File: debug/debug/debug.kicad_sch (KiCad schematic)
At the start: 2 parts

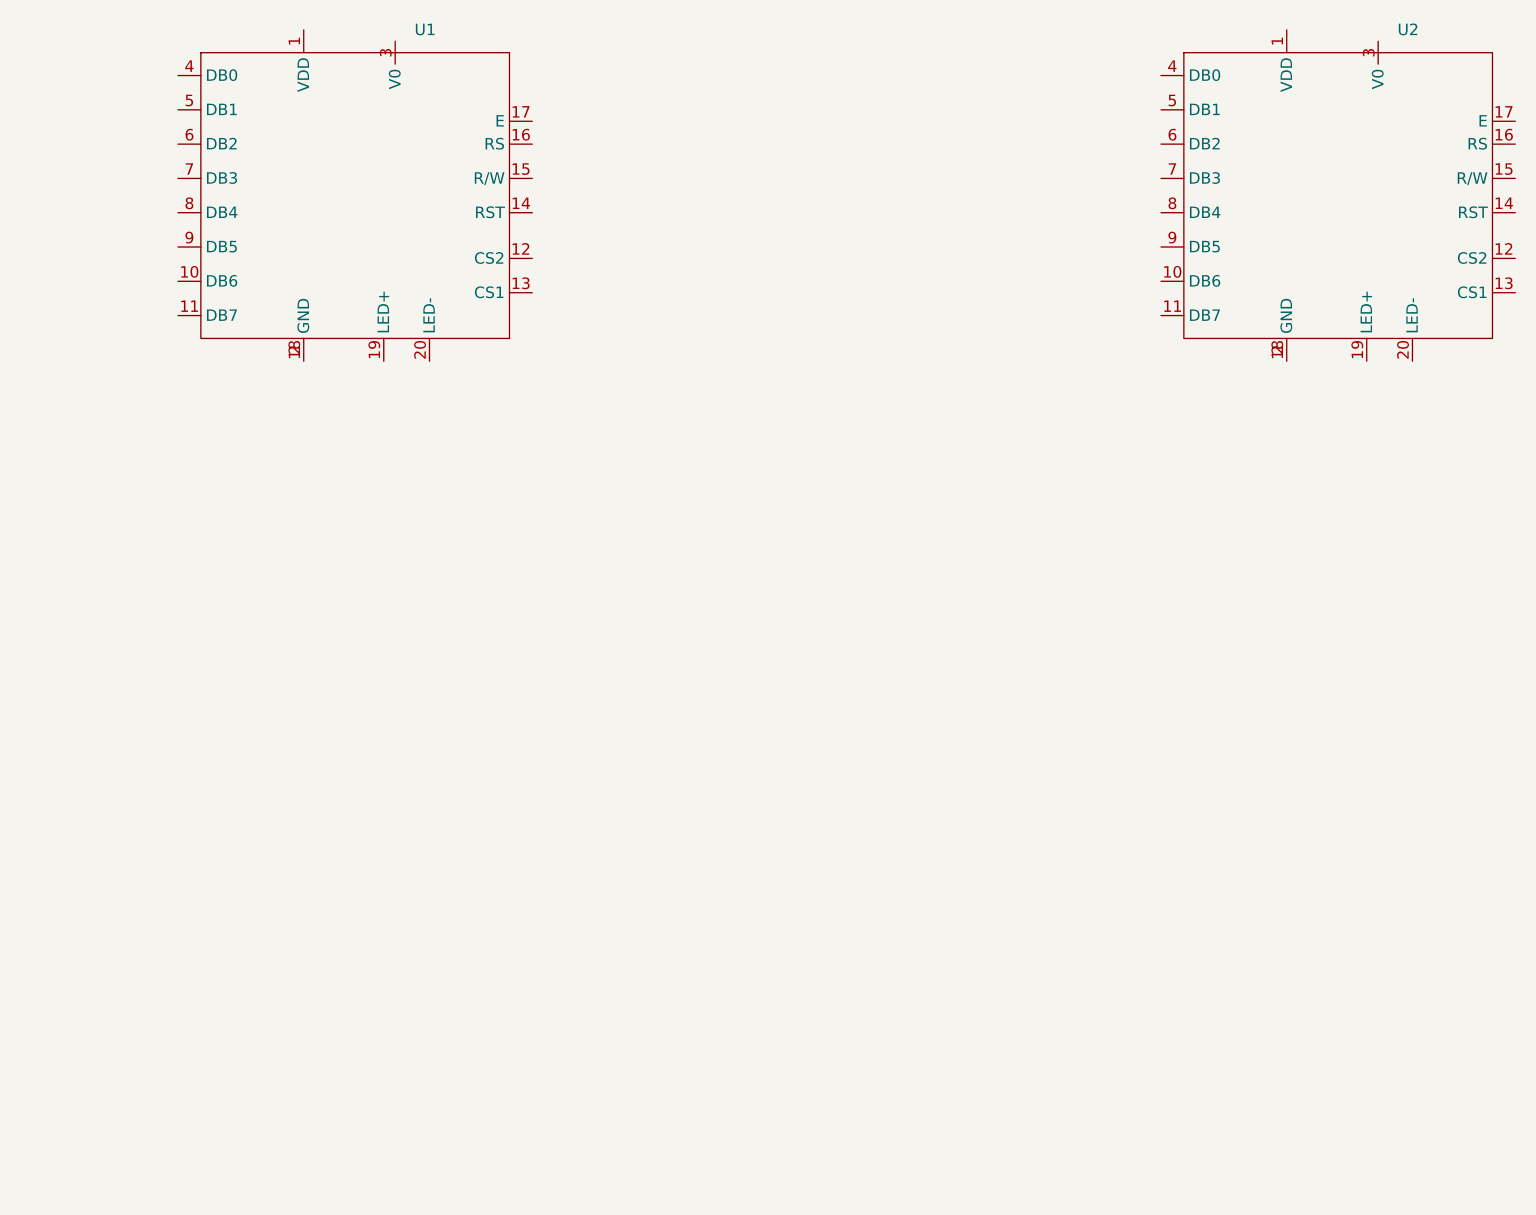
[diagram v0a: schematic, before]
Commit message: Added hierarchial blocks.
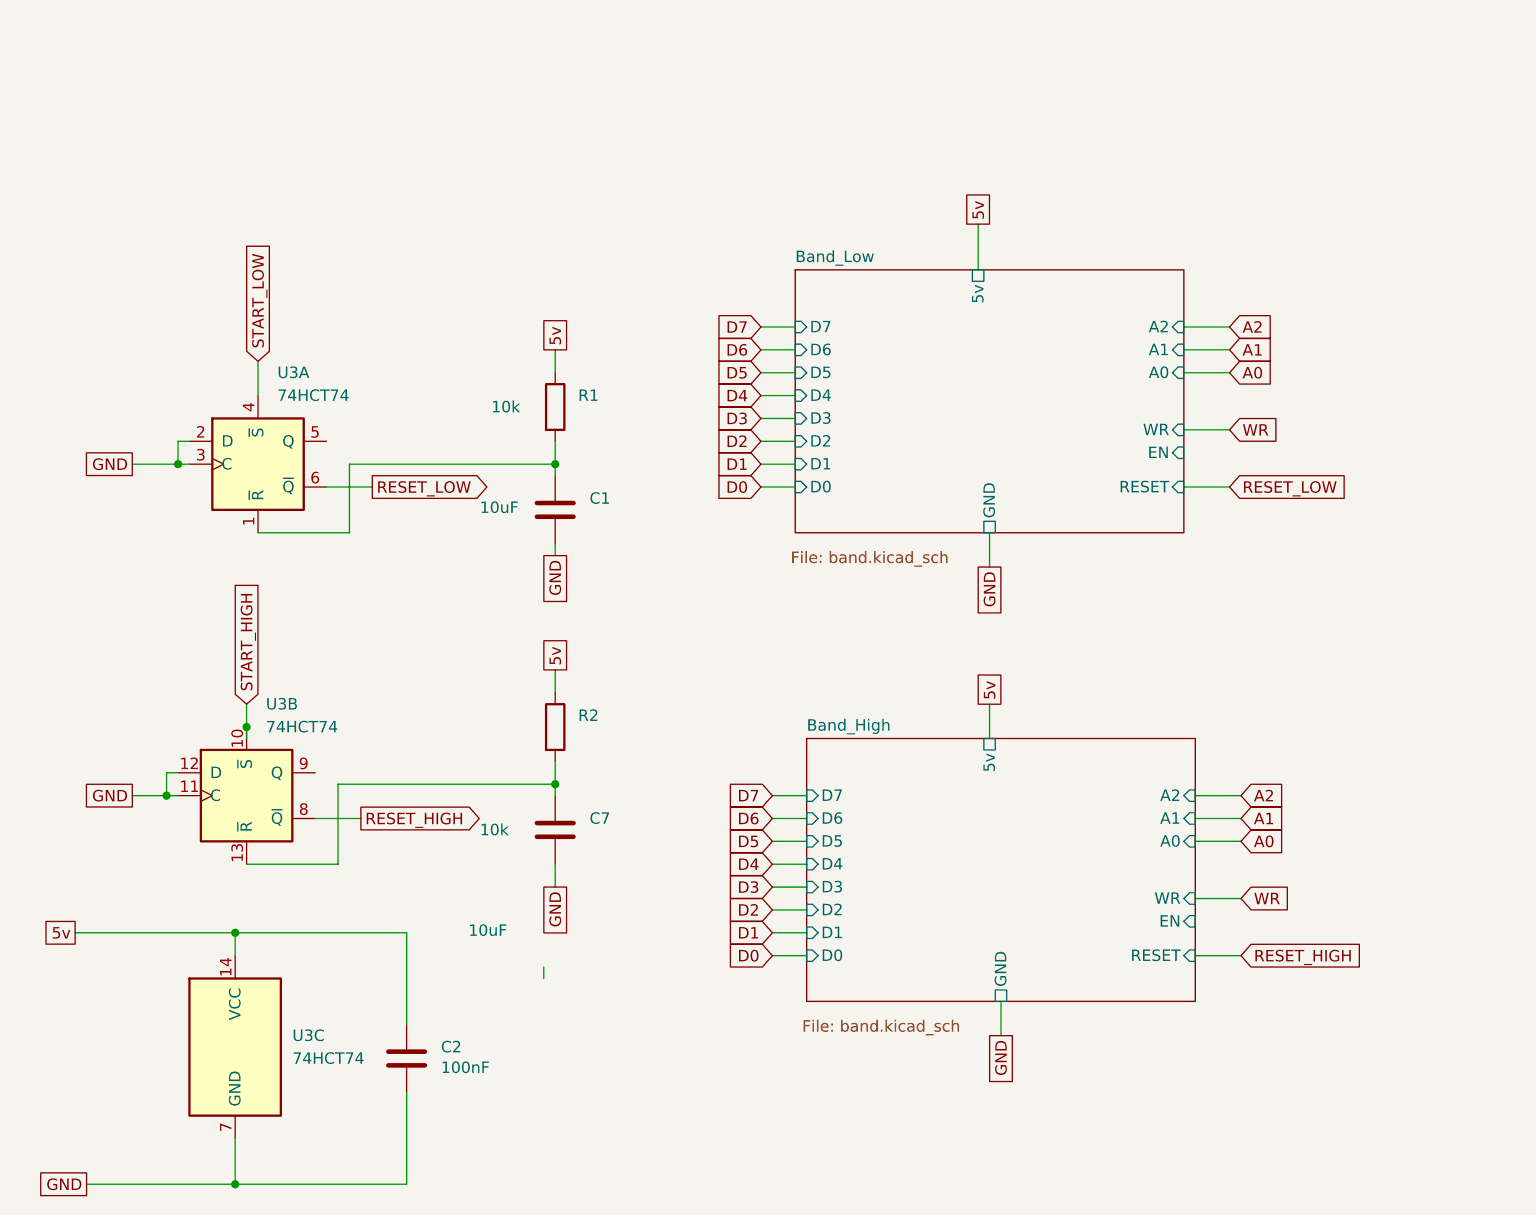
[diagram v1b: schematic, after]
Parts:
- removed U1, U2: (no value), custom:LCD, symbol custom:LCD
- added C1, C7: 10uF, Capacitor_SMD:C_0805_2012Metric_Pad1.18x1.45mm_HandSolder, symbol Device:C
- added C2: 100nF, Capacitor_SMD:C_0805_2012Metric_Pad1.18x1.45mm_HandSolder, symbol Device:C
- added R1, R2: 10k, Resistor_SMD:R_0805_2012Metric_Pad1.20x1.40mm_HandSolder, symbol Device:R
- added U3: 74HCT74, Package_SO:SOIC-14_3.9x8.7mm_P1.27mm, symbol 74xx:74LS74
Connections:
- new net: C7.1, R2.2, U3.13 (~{R})
- new net: C1.1, R1.2, U3.1 (~{R})
- new net 5v: C2.1, R1.1, R2.1, U3.14 (VCC)
- new net GND: C1.2, C2.2, C7.2, U3.11 (C), U3.12 (D), U3.2 (D), U3.3 (C), U3.7 (GND)
- new net RESET_HIGH: U3.8 (~{Q})
- new net RESET_LOW: U3.6 (~{Q})
- new net START_HIGH: U3.10 (~{S})
- new net START_LOW: U3.4 (~{S})
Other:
- added sheet Band_High (band.kicad_sch)
- added sheet Band_Low (band.kicad_sch)
